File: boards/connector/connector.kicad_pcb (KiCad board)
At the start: 4 copper layers, 135.9 x 179.4 mm, 43 parts, among them J1 Conn_01x15, J10 Conn_01x07, J11 Conn_01x07, J12 Conn_01x07, J13 Conn_01x07, J14 CDU_Connector, J15 Conn_02x31_Top_Bottom, J2 Conn_01x15, J3 Conn_01x15, J4 Conn_01x15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

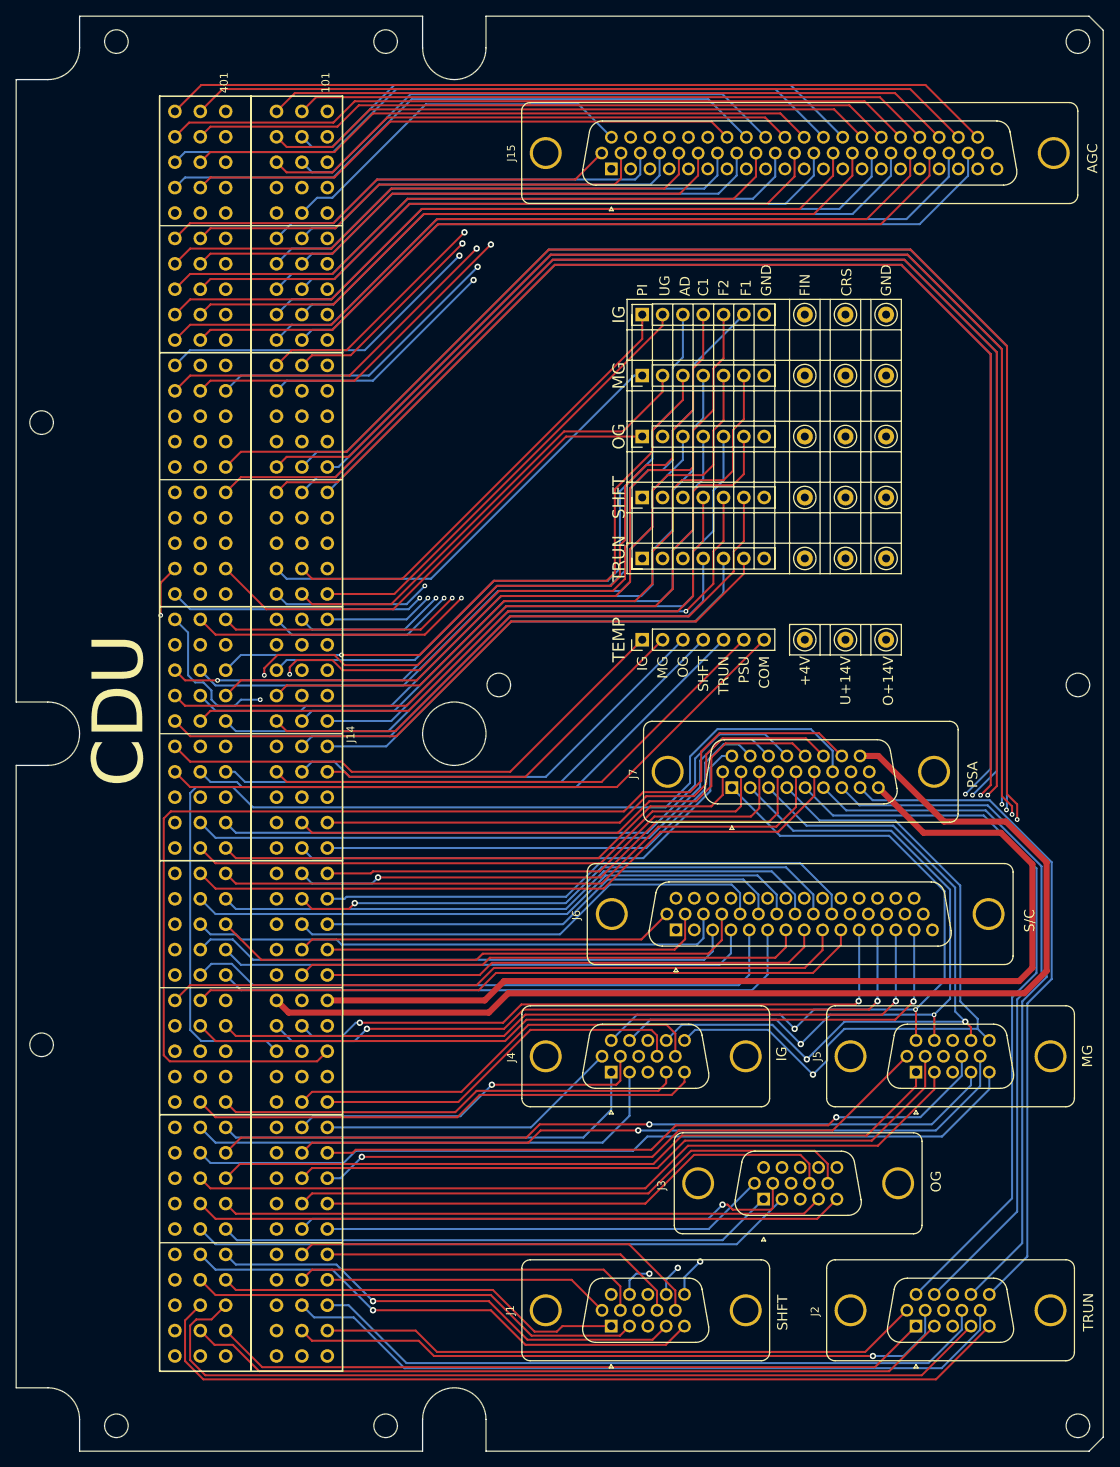
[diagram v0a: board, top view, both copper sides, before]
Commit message: Connector board: swap PSA connector for 44-pin, separate resolver and CDU references, and add some more power pins
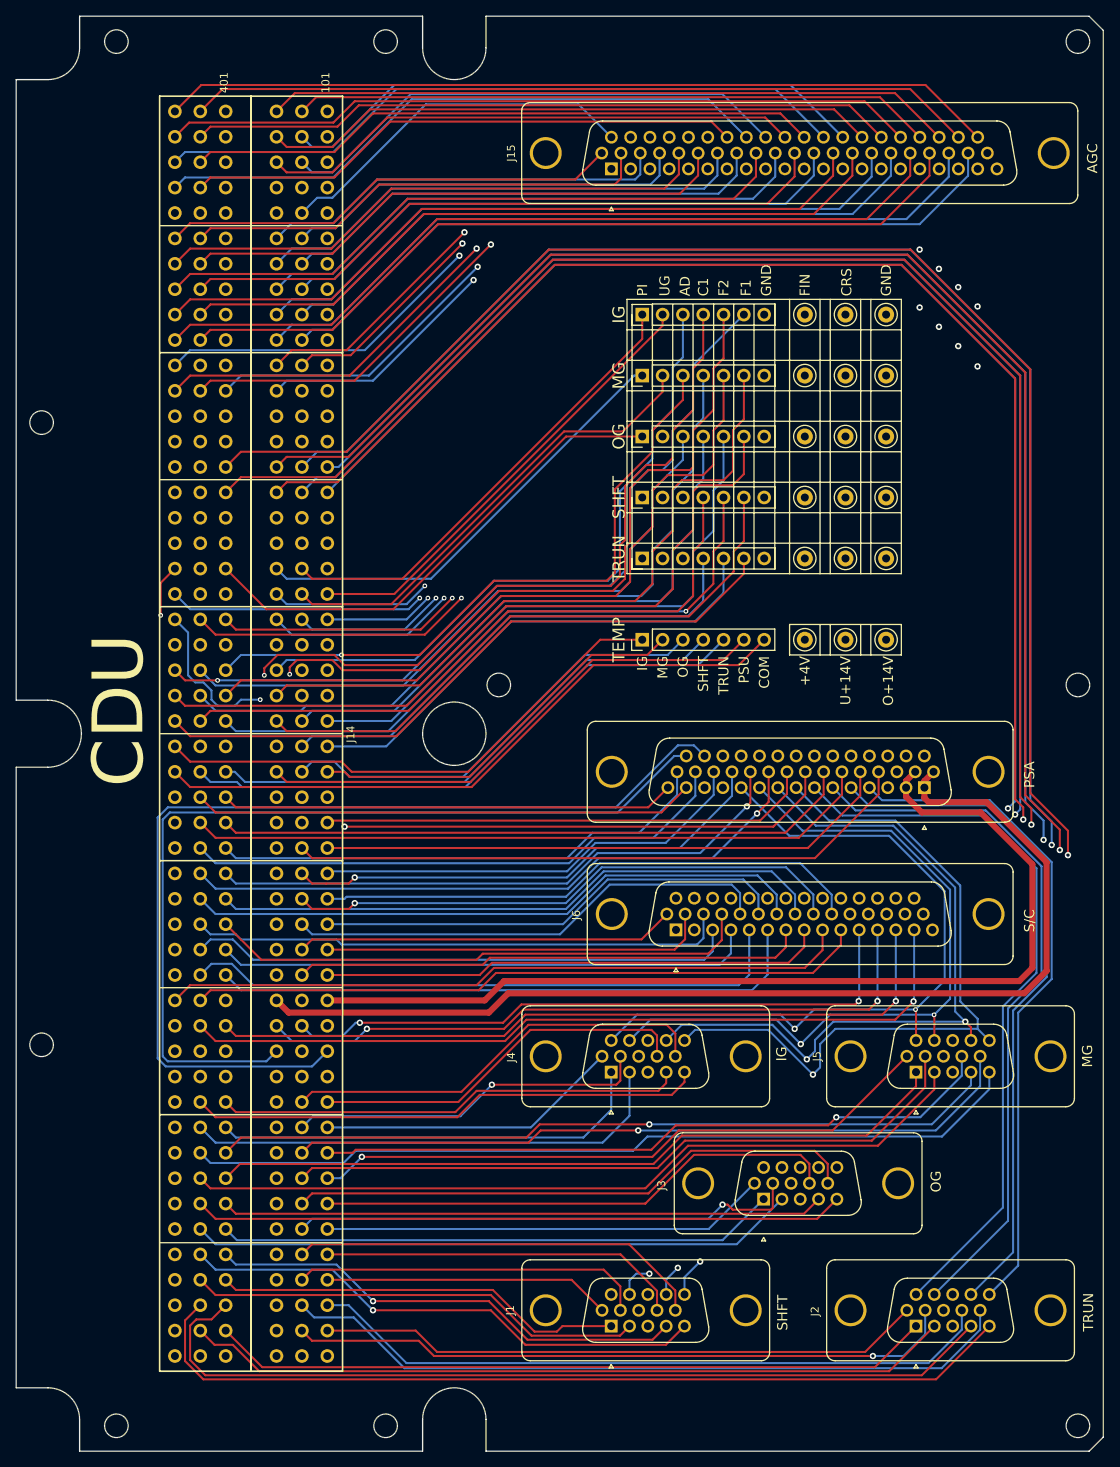
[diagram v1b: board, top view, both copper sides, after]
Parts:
- J7: value Conn_01x26 -> Conn_02x22_Top_Bottom; footprint Connector_Dsub:DSUB-26-HD_Female_Vertical_P2.29x1.98mm_MountingHoles -> Connector_Dsub:DSUB-44-HD_Male_Vertical_P2.29x1.98mm_MountingHoles
- moved J7 24.1 mm to (131.8, 109.9)
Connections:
- J1 pad 11: /O28RFH -> /RO28RFH
- J1 pad 12: /O28RFL -> /RO28RFL
- J1 pad 14: /O5RFH -> /RO5RFH
- J1 pad 15: /O5RFL -> /RO5RFL
- J15 pad 17: unconnected-(J15-Pin_17-Pad17) -> /AGCPSA1
- J15 pad 18: unconnected-(J15-Pin_18-Pad18) -> /AGCPSA2
- J15 pad 19: unconnected-(J15-Pin_19-Pad19) -> /AGCPSA3
- J15 pad 20: unconnected-(J15-Pin_20-Pad20) -> /AGCPSA4
- J2 pad 11: /O28RFH -> /RO28RFH
- J2 pad 12: /O28RFL -> /RO28RFL
- J2 pad 14: /O5RFH -> /RO5RFH
- J2 pad 15: /O5RFL -> /RO5RFL
- J3 pad 11: /U28RFH -> /RU28RFH
- J3 pad 12: /U28RFL -> /RU28RFL
- J3 pad 14: /U5RFH -> /RU5RFH
- J3 pad 15: /U5RFL -> /RU5RFL
- J4 pad 11: /U28RFH -> /RU28RFH
- J4 pad 12: /U28RFL -> /RU28RFL
- J4 pad 14: /U5RFH -> /RU5RFH
- J4 pad 15: /U5RFL -> /RU5RFL
- J5 pad 11: /U28RFH -> /RU28RFH
- J5 pad 12: /U28RFL -> /RU28RFL
- J5 pad 14: /U5RFH -> /RU5RFH
- J5 pad 15: /U5RFL -> /RU5RFL
- J7 pad 1: /U28RFH -> /O+28VH
- J7 pad 10: /ACAEHI -> /RU28RFL
- J7 pad 11: /ACAELO -> /RU28RFH
- J7 pad 12: /BCAEHI -> /O28RFL
- J7 pad 13: /BCAELO -> /O28RFH
- J7 pad 14: /CCAEHI -> /U28RFL
- J7 pad 15: /CCAELO -> /U28RFH
- J7 pad 16: /CAGE -> /O+28VH
- J7 pad 17: GND -> /U+28VH
- J7 pad 2: /U28RFL -> /U+28VH
- J7 pad 25: /CARPSA -> /CCAELO
- J7 pad 26: /O+28VH -> /CCAEHI
- J7 pad 3: /U5RFH -> GND
- J7 pad 4: /U5RFL -> /RO5RFL
- J7 pad 5: /O28RFH -> /RO5RFH
- J7 pad 6: /O28RFL -> /RO28RFL
- J7 pad 7: /O5RFH -> /RO28RFH
- J7 pad 8: /O5RFL -> /RU5RFL
- J7 pad 9: /U+28VH -> /RU5RFH
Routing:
- net /O28RFH: track 197.4 -> 51.9 mm
- net /O28RFL: track 202.0 -> 57.9 mm, vias 1 -> 0
- net /RO28RFH: track 0.00 -> 131.8 mm
- net /RO28RFL: track 0.00 -> 130.5 mm, vias 0 -> 1
- net /O5RFH: track 129.2 -> 0.00 mm, vias 1 -> 0
- net /RO5RFH: track 0.00 -> 128.0 mm, vias 0 -> 1
- net /O5RFL: track 127.8 -> 0.00 mm, vias 1 -> 0
- net /RO5RFL: track 0.00 -> 126.7 mm, vias 0 -> 1
- net /U28RFH: track 173.4 -> 56.8 mm, vias 2 -> 0
- net /U28RFL: track 176.1 -> 62.8 mm, vias 2 -> 0
- net /RU28RFH: track 0.00 -> 111.0 mm, vias 0 -> 2
- net /RU28RFL: track 0.00 -> 107.1 mm, vias 0 -> 2
- net /U5RFH: track 104.5 -> 0.00 mm, vias 2 -> 0
- net /RU5RFH: track 0.00 -> 104.1 mm, vias 0 -> 2
- net /U5RFL: track 103.4 -> 0.00 mm, vias 1 -> 0
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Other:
- outline, holes or cut-outs redrawn
